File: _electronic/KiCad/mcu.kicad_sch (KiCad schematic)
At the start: 3 parts

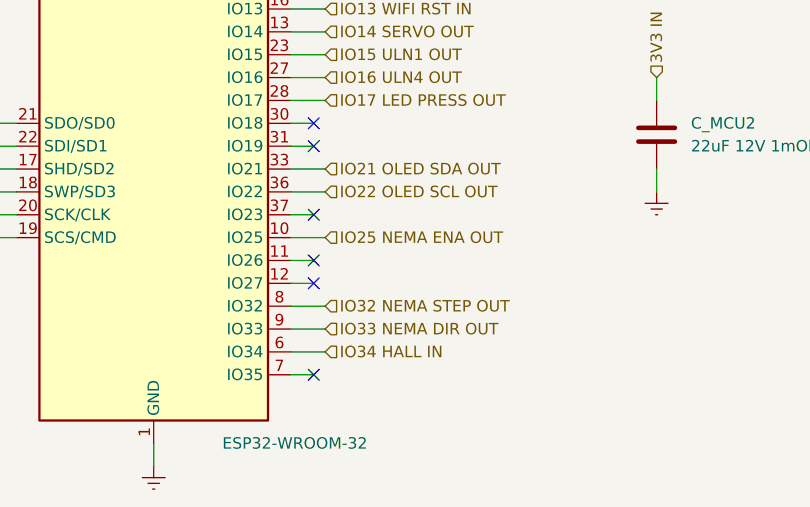
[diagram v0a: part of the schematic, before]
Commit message: added buzzer
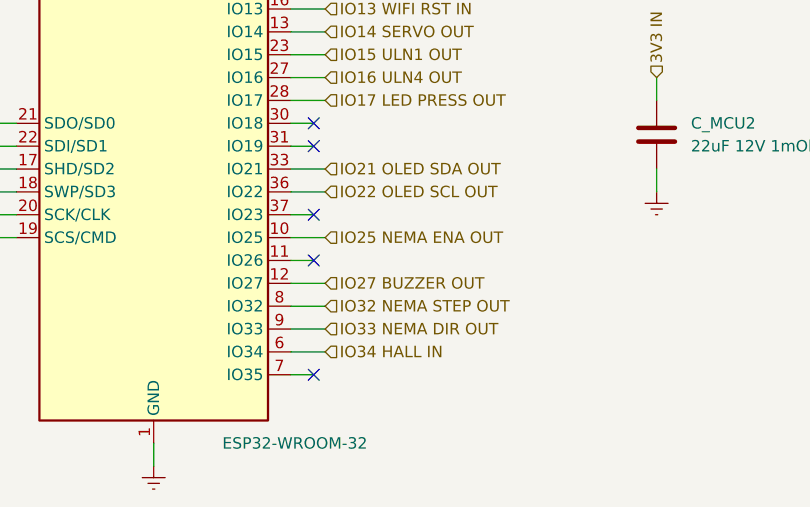
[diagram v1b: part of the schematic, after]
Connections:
- net IO27 BUZZER OUT: now reaches U_MCU1.12 (IO27)
- no-connect marks 15 -> 14
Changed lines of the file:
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@@
   (no_connect (at 158.75 115.57))
   (no_connect (at 123.19 105.41))
-  (no_connect (at 158.75 123.19))
   (wire (pts (xy 160.02 92.71) (xy 156.21 92.71))
     (stroke (width 0) (type default) (color 0 0 0 0))
@@
   )
   (wire (pts (xy 158.75 115.57) (xy 156.21 115.57))
-    (stroke (width 0) (type default) (color 0 0 0 0))
-  )
-  (wire (pts (xy 158.75 123.19) (xy 156.21 123.19))
     (stroke (width 0) (type default) (color 0 0 0 0))
   )
@@
   )
   (wire (pts (xy 140.97 67.31) (xy 140.97 69.85))
+    (stroke (width 0) (type default) (color 0 0 0 0))
+  )
+  (wire (pts (xy 156.21 123.19) (xy 160.02 123.19))
     (stroke (width 0) (type default) (color 0 0 0 0))
   )
@@
     (effects (font (size 1.27 1.27)) (justify left))
   )
+  (hierarchical_label "IO27 BUZZER OUT" (shape input) (at 160.02 123.19 0)
+    (effects (font (size 1.27 1.27)) (justify left))
+  )

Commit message: schematics footer and export
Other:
- company: (none) -> Andrei Speridiao
- title: (none) -> E-TKT
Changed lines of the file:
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@@
 (kicad_sch (version 20211123) (generator eeschema)
   (paper "A4")
+  (title_block
+    (title "E-TKT")
+    (date "2022-07-21")
+    (rev "3")
+    (company "Andrei Speridiao")
+  )
   (no_connect (at 123.19 115.57))
   (no_connect (at 158.75 90.17))
